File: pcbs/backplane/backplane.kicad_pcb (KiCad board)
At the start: 2 copper layers, 80 x 50 mm, 11 parts, among them P1 CONN_02X04, P2 CONN_02X04, P3 USB_B, P4 CONN_02X09, P5 CONN_02X09, U1 FT232RL

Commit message: Mechanical specs updated.
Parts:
- removed the REF** at (95.0, 125.0)
- removed the REF** at (100.0, 80.0)
- removed the REF** at (100.0, 120.0)
- removed the REF** at (170.0, 120.0)
- removed the REF** at (170.0, 80.0)
- added REF**: EuroBoard_viertel_Type-I_80mmX50mm_holes, EuroBoard_Outline:EuroBoard_viertel_Type-I_80mmX50mm_holes, F.Cu at (110.0, 120.0)
- P1, P2: value CONN_02X04 -> CONN_02X03; footprint Pin_Headers:Pin_Header_Straight_2x04 -> Pin_Headers:Pin_Header_Straight_2x03
- P4, P5: value CONN_02X09 -> CONN_02X07; footprint Pin_Headers:Pin_Header_Straight_2x09 -> Pin_Headers:Pin_Header_Straight_2x07
- U1: value FT232RL -> CH340G; footprint Housings_SSOP:SSOP-28_5.3x10.2mm_Pitch0.65mm -> SMD_Packages:SO-16-N
- moved P4 36.1 mm to (165.0, 87.7)
- moved P1 33.5 mm to (120.0, 80.0)
- moved P5 25.0 mm to (165.0, 112.7)
- moved U1 22.4 mm to (150.0, 90.0), turned to 270 degrees
- moved P2 21.2 mm to (120.0, 105.0)
- moved P3 11.2 mm to (115.0, 85.0), turned to 270 degrees
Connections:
- net PWM1 renamed GPIO0
- net SPI_CS renamed UART_RX
- net VCC renamed 5V
- P1 pad 4: GND -> ADC3
- P1 pad 6: DAC1 -> ADC4
- P2 pad 4: GND -> ADC3
- P2 pad 6: DAC1 -> ADC4
- P4 pad 10: GPIO1 -> GPIO4
- P4 pad 12: GPIO2 -> nRST
- P4 pad 13: I2C_SCL -> DAC1
- P4 pad 14: GPIO3 -> DAC2
- P4 pad 4: PWM2 -> GPIO1
- P4 pad 5: SPI_CLK -> I2C_SCL
- P4 pad 6: DAC1 -> GPIO2
- P4 pad 7: SPI_MISO -> I2C_SDA
- P4 pad 8: DAC2 -> GPIO3
- P4 pad 9: SPI_MOSI -> UART_TX
- P5 pad 10: GPIO1 -> GPIO4
- P5 pad 12: GPIO2 -> nRST
- P5 pad 13: I2C_SCL -> DAC1
- P5 pad 14: GPIO3 -> DAC2
- P5 pad 4: PWM2 -> GPIO1
- P5 pad 5: SPI_CLK -> I2C_SCL
- P5 pad 6: DAC1 -> GPIO2
- P5 pad 7: SPI_MISO -> I2C_SDA
- P5 pad 8: DAC2 -> GPIO3
- P5 pad 9: SPI_MOSI -> UART_TX
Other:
- board text added: "The boards, which are plugged in should have the right angeled mates at the edge."
- board text added: "This is the distance one has between the two boards minus the board thickness and the highest component."

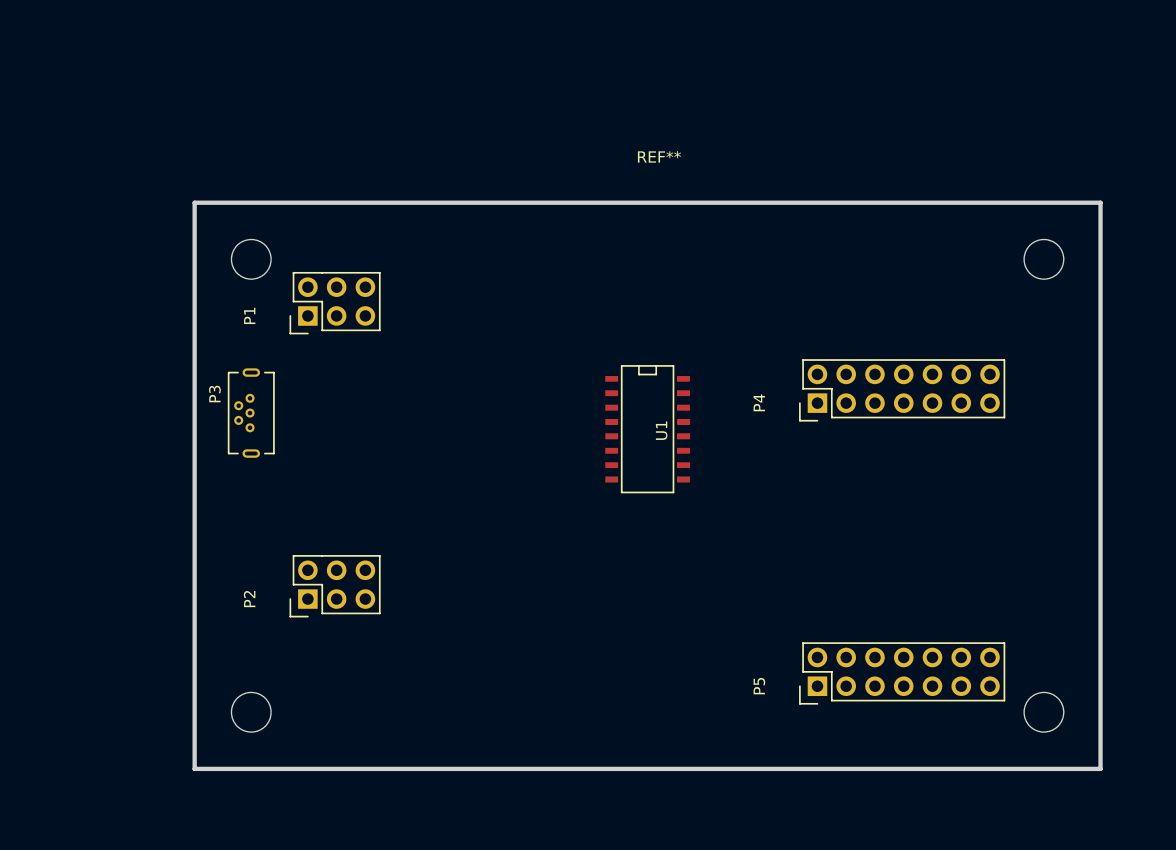
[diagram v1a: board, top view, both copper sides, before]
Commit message: Came quite far with backplane design. Not finished yet.
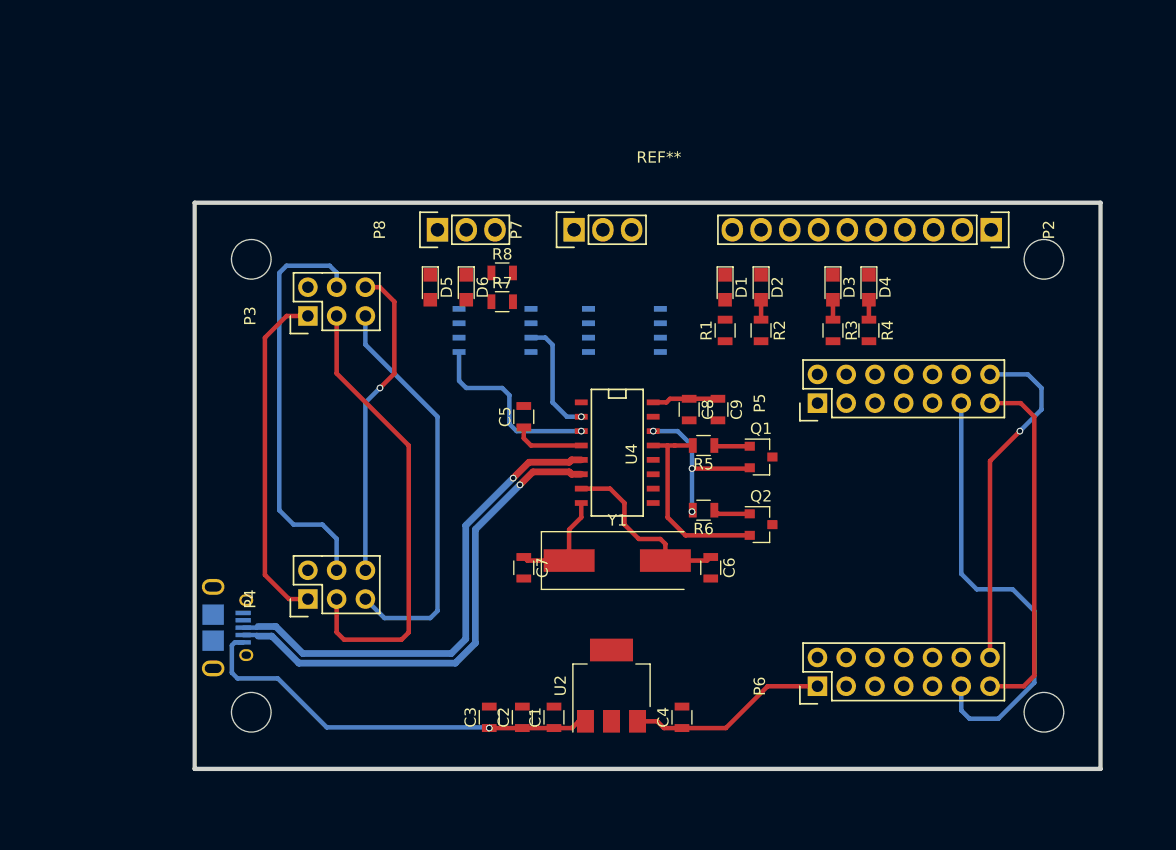
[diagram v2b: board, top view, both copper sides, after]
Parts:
- removed the P3 at (115.0, 85.0)
- added C1: 10u, Resistors_SMD:R_0805, F.Cu at (141.7, 115.4)
- added C2: 1u, Resistors_SMD:R_0805, F.Cu at (138.9, 115.4)
- added C3: 100n, Resistors_SMD:R_0805, F.Cu at (136.0, 115.4)
- added C4: 1u, Resistors_SMD:R_0805, F.Cu at (153.0, 115.4)
- added C5: 100n, Resistors_SMD:R_0805, F.Cu at (139.1, 88.9)
- added C6: 22p, Resistors_SMD:R_0805, F.Cu at (155.6, 102.2)
- added C7: 22p, Resistors_SMD:R_0805, F.Cu at (139.1, 102.2)
- added C8: 1u, Resistors_SMD:R_0805, F.Cu at (153.7, 88.3)
- added C9: 100n, Resistors_SMD:R_0805, F.Cu at (156.2, 88.3)
- added D1: LED, LEDs:LED_0805, F.Cu at (156.8, 77.5)
- added D2: LED, LEDs:LED_0805, F.Cu at (160.0, 77.5)
- added D3: LED, LEDs:LED_0805, F.Cu at (166.4, 77.5)
- added D4: LED, LEDs:LED_0805, F.Cu at (169.5, 77.5)
- added D5: LED, LEDs:LED_0805, F.Cu at (130.8, 77.5)
- added D6: LED, LEDs:LED_0805, F.Cu at (134.0, 77.5)
- added P1: USB_B, myUSB:ZX62D-B-5P8(30), B.Cu at (111.6, 111.1)
- added P2: CONN_01X10, mySamtec:Samtec-PHT-1-9-01-L-S, F.Cu at (180.3, 72.4)
- added P7: CONN_01X03, mySamtec:Samtec-PHT-1-3-01-L-S, F.Cu at (143.5, 72.4)
- added P8: CONN_01X03, mySamtec:Samtec-PHT-1-3-01-L-S, F.Cu at (131.4, 72.4)
- added Q1: MMBT3904, SOT-23, F.Cu at (160.0, 92.5)
- added Q2: MMBT3904, SOT-23, F.Cu at (160.0, 98.4)
- added R1: 1k, Resistors_SMD:R_0805, F.Cu at (156.8, 81.3)
- added R2: 1k, Resistors_SMD:R_0805, F.Cu at (160.0, 81.3)
- added R3: 1k, Resistors_SMD:R_0805, F.Cu at (166.4, 81.3)
- added R4: 1k, Resistors_SMD:R_0805, F.Cu at (169.5, 81.3)
- added R5: 10k, Resistors_SMD:R_0805, F.Cu at (154.9, 91.4)
- added R6: 10k, Resistors_SMD:R_0805, F.Cu at (154.9, 97.2)
- added R7: 1k, Resistors_SMD:R_0805, F.Cu at (137.2, 78.7)
- added R8: 1k, Resistors_SMD:R_0805, F.Cu at (137.2, 76.2)
- added U1: LM358, SMD_Packages:SOIC-8-N, B.Cu at (136.5, 81.3)
- added U2: TC1262-33VDB, SOT-223, F.Cu at (146.8, 112.6)
- added U3: LM358, SMD_Packages:SOIC-8-N, B.Cu at (148.0, 81.3)
- added Y1: Crystal, Crystals:Crystal_SMD_HC49-SD, F.Cu at (147.3, 101.6)
- moved U4 3.39 mm to (147.3, 92.1)
- renumbered P1 to P3, P2 to P4, P4 to P5, P5 to P6, U1 to U4
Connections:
- P5 pad 1: 5V -> 3.3V
- P6 pad 1: 5V -> 3.3V
- U4 pad 1: (no net) -> GND
- U4 pad 13: (no net) -> DTR
- U4 pad 14: (no net) -> RTS
- U4 pad 16: (no net) -> 3.3V
- U4 pad 2: (no net) -> UART_RX
- U4 pad 3: (no net) -> UART_TX
- U4 pad 4: (no net) -> 3.3V
- U4 pad 5: (no net) -> D+
- U4 pad 6: (no net) -> D-
- U4 pad 7: (no net) -> Net-(C6-Pad1)
- U4 pad 8: (no net) -> Net-(C7-Pad1)
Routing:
- net 5V: track 0.00 -> 67.7 mm, vias 0 -> 1
- net UART_RX: track 0.00 -> 49.7 mm, vias 0 -> 1
- net D+: track 0.00 -> 43.9 mm, vias 0 -> 1
- net D-: track 0.00 -> 43.9 mm, vias 0 -> 1
- net ADC1: track 0.00 -> 40.4 mm
- net ADC3: track 0.00 -> 36.7 mm
- net ADC2: track 0.00 -> 36.0 mm, vias 0 -> 1
- net DAC1: track 0.00 -> 31.6 mm
- net DAC2: track 0.00 -> 30.7 mm, vias 0 -> 1
- net 3.3V: track 0.00 -> 29.8 mm
- net ADC4: track 0.00 -> 27.9 mm, vias 0 -> 1
- net DTR: track 0.00 -> 17.8 mm
- net UART_TX: track 0.00 -> 16.7 mm, vias 0 -> 1
- net Net-(C6-Pad1): track 0.00 -> 16.2 mm
- net RTS: track 0.00 -> 15.1 mm, vias 0 -> 3
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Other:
- rule via_min_drill: 0.3 -> 0.2
- board text added: "Analog PCB"
- board text added: "Digital PCB"

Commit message: Backplane version 1 ready.
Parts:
- removed P2: CONN_01X10, mySamtec:Samtec-PHT-1-9-01-L-S
- added 3V3: TEST, myTestPoints:TP_SMD_quadr_1mm, F.Cu at (148.2, 113.7)
- added 5V0: TEST, myTestPoints:TP_SMD_quadr_1mm, F.Cu at (168.3, 112.7)
- added ADC1: TEST, myTestPoints:TP_SMD_quadr_1mm, F.Cu at (125.2, 80.7)
- added ADC2: TEST, myTestPoints:TP_SMD_quadr_1mm, F.Cu at (128.1, 80.7)
- added ADC3: TEST, myTestPoints:TP_SMD_quadr_1mm, F.Cu at (126.9, 70.6)
- added ADC4: TEST, myTestPoints:TP_SMD_quadr_1mm, F.Cu at (129.4, 70.6)
- added DAC1: TEST, myTestPoints:TP_SMD_quadr_1mm, F.Cu at (187.8, 84.0)
- added DAC2: TEST, myTestPoints:TP_SMD_quadr_1mm, F.Cu at (184.9, 78.2)
- added G***: LOGO, myPics:uppsense_logo, F.Cu at (153.8, 93.4)
- added G***: LOGO, myPics:uu_logo, B.Cu at (176.7, 92.8)
- added GND, GND1: TEST, myTestPoints:TP_SMD_quadr_3mm, F.Cu at (169.5, 68.0)
- added Q3: Si2323, TO_SOT_Packages_SMD:SOT-23, B.Cu at (124.1, 109.4)
- added REF**: Stitching-Via-0.5-0.7, myVias:Stitchging-Via-0.4-0.7, F.Cu at (148.8, 105.6)
- added REF**: Stitching-Via-0.5-0.7, myVias:Stitchging-Via-0.4-0.7, F.Cu at (143.5, 105.6)
- added REF**: Stitching-Via-0.5-0.7, myVias:Stitchging-Via-0.4-0.7, F.Cu at (145.7, 102.3)
- added SCL1: TEST, myTestPoints:TP_SMD_quadr_1mm, F.Cu at (175.9, 86.8)
- added SDA1: TEST, myTestPoints:TP_SMD_quadr_1mm, F.Cu at (178.2, 86.8)
- C1, C2, C3, C4, C5, C6, C7, C8, C9, Q1, Q2, R1, R2, R3, R4, R5, R6, R7, R8, U2, U4, Y1: moved to B.Cu
- moved Q1 25.0 mm to (135.9, 85.8), turned to 90 degrees
- moved C3 24.9 mm to (160.7, 111.8)
- moved C2 24.6 mm to (163.2, 111.8)
- moved C1 24.3 mm to (165.8, 111.8)
- moved Q2 22.3 mm to (141.6, 85.8), turned to 90 degrees
- moved R5 19.7 mm to (135.3, 91.5), turned to 270 degrees
- moved P8 18.2 mm to (149.3, 68.6)
- moved U1 17.3 mm to (153.7, 83.2)
- moved C5 16.7 mm to (141.0, 105.4), turned to 270 degrees
- moved R6 15.1 mm to (141.0, 91.5), turned to 270 degrees
- moved C7 13.0 mm to (130.2, 111.8)
- moved C6 13.0 mm to (146.7, 111.8)
- moved Y1 13.0 mm to (138.5, 111.2)
- moved U3 12.3 mm to (153.7, 92.1)
- moved D1 12.1 mm to (145.4, 73.6), turned to 90 degrees
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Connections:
- D1 pad 1: LED_5V -> Net-(D1-Pad1)
- D1 pad 2: Net-(D1-Pad2) -> LED_5V
- D2 pad 1: LED_5V -> Net-(D2-Pad1)
- D2 pad 2: Net-(D2-Pad2) -> LED_5V
- D3 pad 1: LED_5V -> Net-(D3-Pad1)
- D3 pad 2: Net-(D3-Pad2) -> LED_5V
- D4 pad 1: LED_5V -> Net-(D4-Pad1)
- D4 pad 2: Net-(D4-Pad2) -> LED_5V
- P1 pad 1: 5V -> Net-(P1-Pad1)
- P6 pad 11: UART_RX -> (no net)
- P6 pad 12: nRST -> (no net)
- P6 pad 2: GPIO0 -> (no net)
- P6 pad 9: UART_TX -> (no net)
- R1 pad 1: Net-(D1-Pad2) -> Net-(D1-Pad1)
- R2 pad 1: Net-(D2-Pad2) -> Net-(D2-Pad1)
- R3 pad 1: Net-(D3-Pad2) -> Net-(D3-Pad1)
- R4 pad 1: Net-(D4-Pad2) -> Net-(D4-Pad1)
- U4 pad 2: UART_RX -> UART_TX
- U4 pad 3: UART_TX -> UART_RX
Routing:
- net 3.3V: track 29.8 -> 157.5 mm, vias 0 -> 6
- net I2C_SDA: track 0.00 -> 107.0 mm, vias 0 -> 2
- net I2C_SCL: track 0.00 -> 77.2 mm, vias 0 -> 2
- net nRST: track 0.00 -> 71.9 mm
- net 5V: track 67.7 -> 127.3 mm, vias 1 -> 2
- net GPIO3: track 0.00 -> 58.6 mm, vias 0 -> 1
- net LED_5V: track 0.00 -> 57.8 mm, vias 0 -> 3
- net GPIO4: track 0.00 -> 56.4 mm, vias 0 -> 1
- net UART_TX: track 16.7 -> 69.8 mm, vias 1 -> 4
- net GPIO1: track 0.00 -> 51.3 mm, vias 0 -> 1
- net GPIO2: track 0.00 -> 47.7 mm
- net GPIO0: track 0.00 -> 44.3 mm, vias 0 -> 1
- net Net-(R1-Pad2): track 0.00 -> 23.5 mm
- net Net-(R4-Pad2): track 0.00 -> 22.0 mm, vias 0 -> 2
- net UART_RX: track 49.7 -> 68.9 mm, vias 1 -> 5
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- added copper zone on B.Cu, net GND
- added copper zone on F.Cu, net GND
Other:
- board text added: "3.3V"
- board text added: "5V"
- board text added: "RX"
- board text added: "SCL"
- board text added: "SDA"
- board text added: "TX"

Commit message: Simulated a lot today. Ideas for the new transimpedance amp. are there.
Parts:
- removed the REF** at (114.5, 116.2)
- added REF**: MountingHole_3.2mm_M3_DIN965, Mounting_Holes:MountingHole_3.2mm_M3_DIN965, F.Cu at (189.5, 111.2)
- added REF**: MountingHole_3.2mm_M3_DIN965, Mounting_Holes:MountingHole_3.2mm_M3_DIN965, F.Cu at (189.5, 71.2)
- added REF**: MountingHole_3.2mm_M3_DIN965, Mounting_Holes:MountingHole_3.2mm_M3_DIN965, F.Cu at (119.5, 71.2)
- added REF**: MountingHole_3.2mm_M3_DIN965, Mounting_Holes:MountingHole_3.2mm_M3_DIN965, F.Cu at (119.5, 111.2)
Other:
- outline, holes or cut-outs redrawn
